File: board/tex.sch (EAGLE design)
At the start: 270 parts, among them K1 HLS8L-DC5V-S-C, K2 HLS8L-DC5V-S-C, K3 HLS8L-DC5V-S-C, K4 HLS8L-DC5V-S-C, Q41 FDD4141, U1 RELAY-S108T02PTH, U12 OPTO-LTV817, U13 OPTO-LTV817, U14 OPTO-LTV817, U15 OPTO-LTV817, U17 24LC32A, U18 IO-HC4051, U2 RELAY-S108T02PTH, U4 AZ23C5V1, Y1 32.768KHz

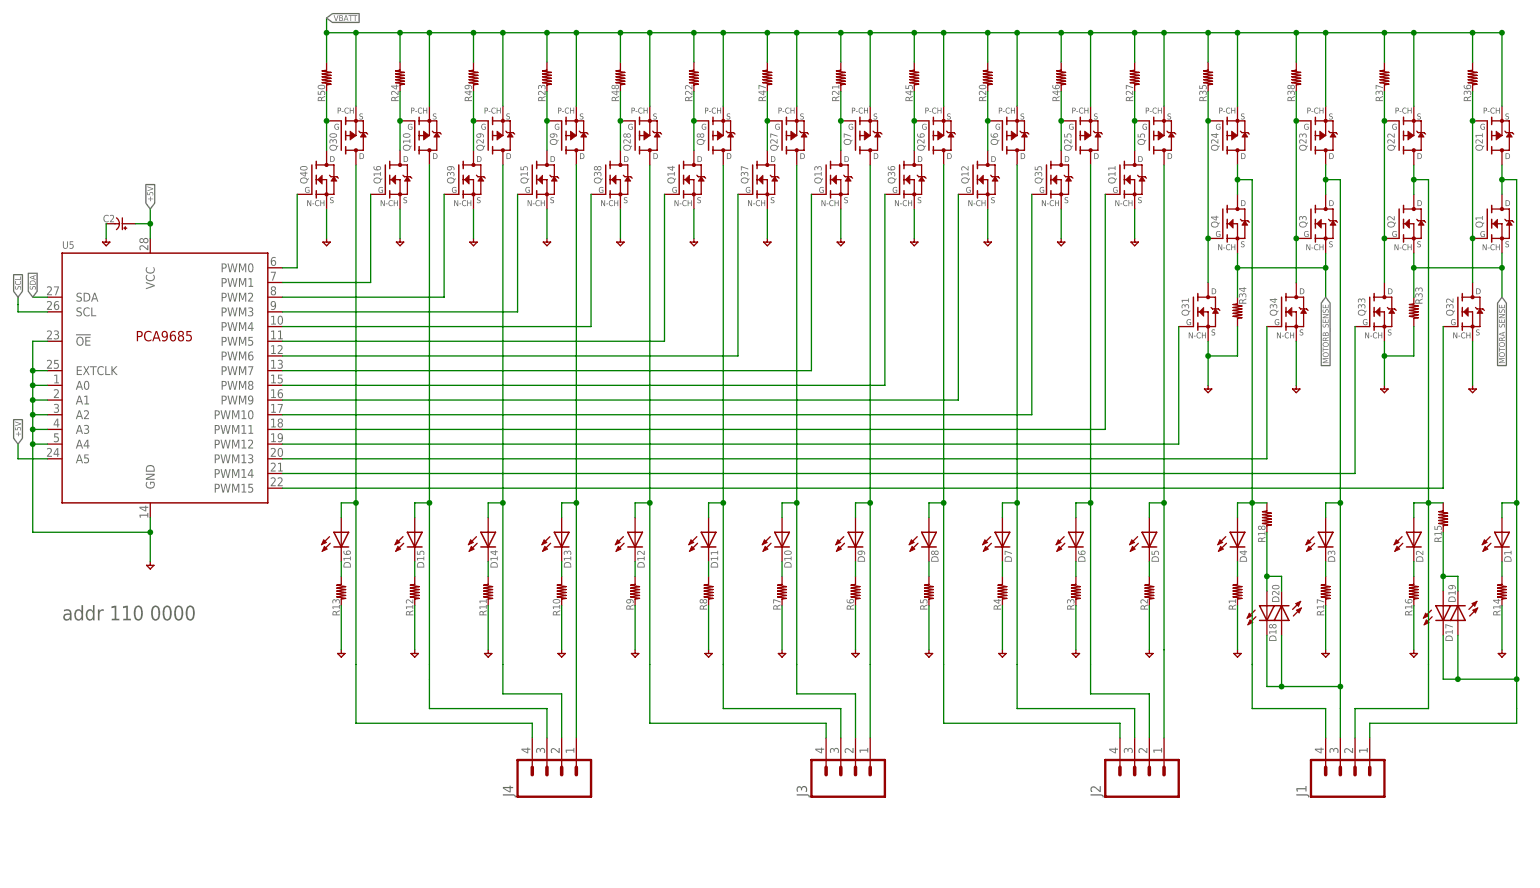
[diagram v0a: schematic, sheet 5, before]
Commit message: set R and C values
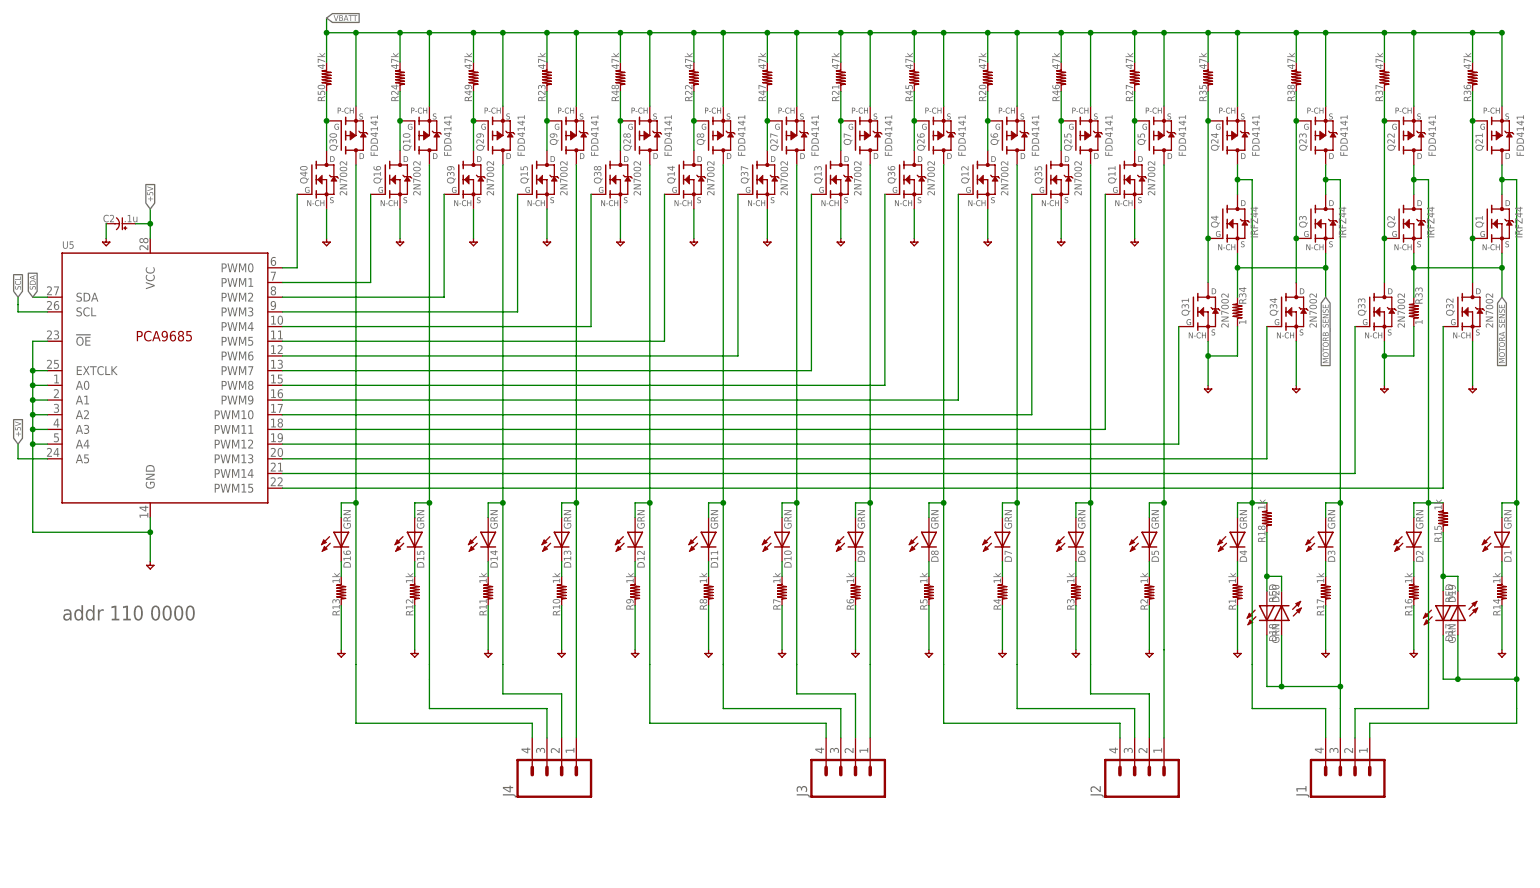
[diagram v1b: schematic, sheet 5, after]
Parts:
- C11, C15, C17, C18, C19, C2, C20, C21, C22, C23, C24, C25, C26, C27, C28, C29, C6, C7: value (none) -> .1u
- C13, C14: value .1u -> 10p
- D1, D10, D11, D12, D13, D14, D15, D16, D19, D2, D20, D25, D26, D27, D28, D29, D3, D30, D32, D4, D5, D6, D7, D8, D9: value (none) -> GRN
- D17, D18, D33: value (none) -> RED
- D21, D22, D23, D24, D35, D36: value (none) -> 1n4148
- D31: value (none) -> VZ=15.0
- D34: value (none) -> BLUE
- Q1, Q2, Q3, Q4: value (none) -> IRFZ44
- Q10, Q21, Q22, Q23, Q24, Q25, Q26, Q27, Q28, Q29, Q30, Q5, Q6, Q7, Q8, Q9: value (none) -> FDD4141
- Q11, Q12, Q13, Q14, Q15, Q16, Q17, Q18, Q19, Q20, Q31, Q32, Q33, Q34, Q35, Q36, Q37, Q38, Q39, Q40, Q42, Q43, Q44, Q45, Q46, Q47: value (none) -> 2N7002
- R1, R10, R11, R12, R13, R14, R15, R16, R17, R18, R2, R29, R3, R30, R31, R32, R4, R5, R58, R59, R6, R65, R66, R67, R68, R7, R8, R9: value (none) -> 1k
- R20, R21, R22, R23, R24, R27, R35, R36, R37, R38, R41, R42, R45, R46, R47, R48, R49, R50, R80, R81, R82, R83, R84, R85, R86, R88: value (none) -> 47k
- R25, R26, R60, R61, R62: value (none) -> 220
- R33, R34: value (none) -> 1
- R51: value (none) -> 10
- R64: value (none) -> 0
- R75: value (none) -> DNP
- R76, R87, R89, R90, R91, R92, R93, R94: value (none) -> 10k
- R78: value (none) -> 100

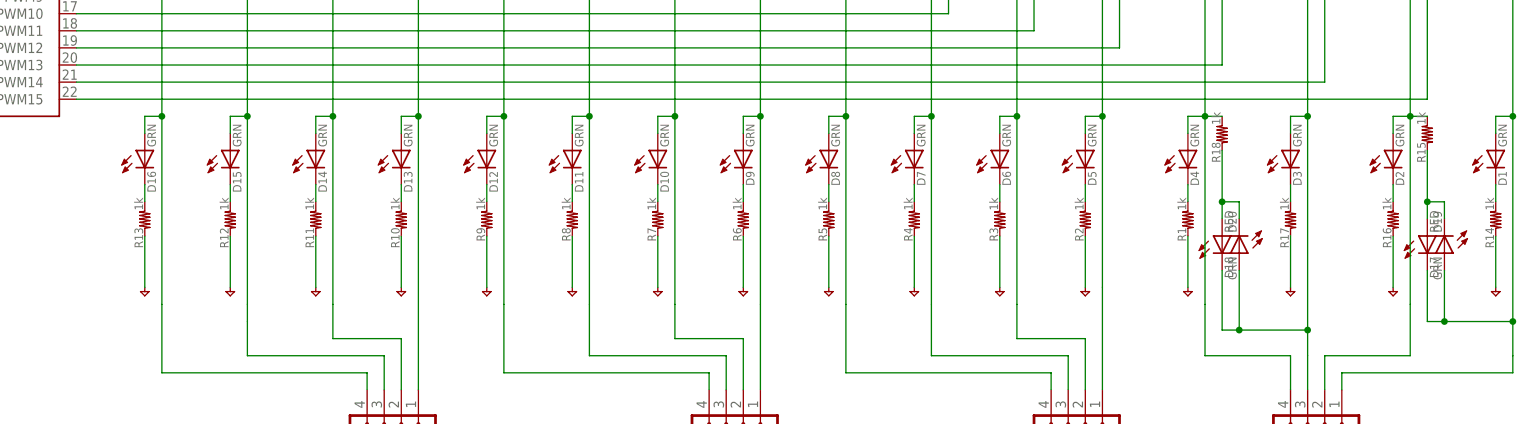
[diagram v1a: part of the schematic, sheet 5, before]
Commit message: changed connectors to match new lib naming
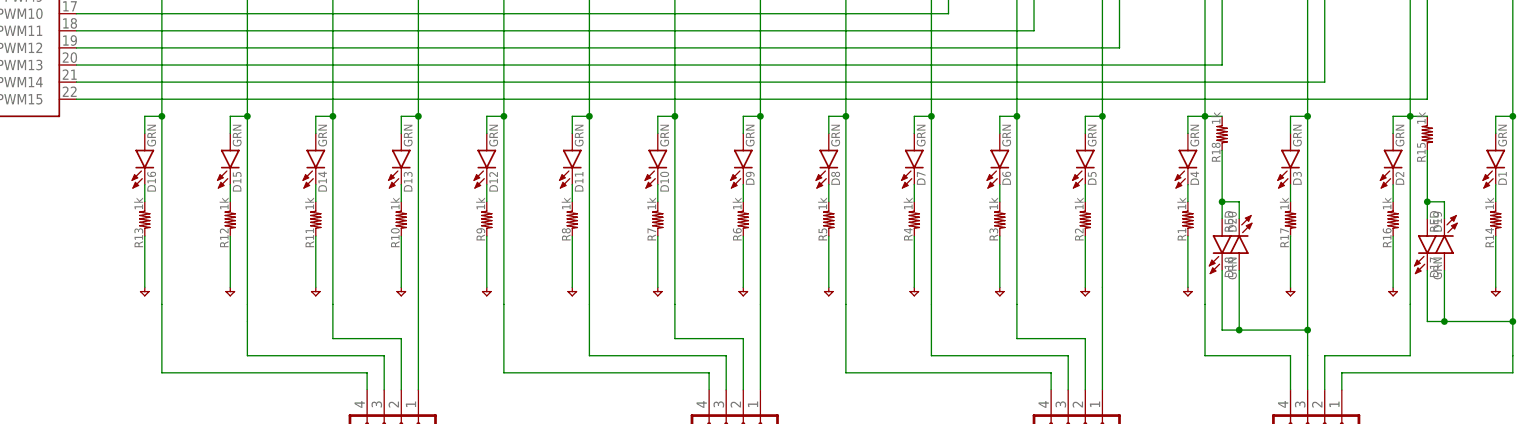
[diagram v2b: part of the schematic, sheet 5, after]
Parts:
- C1, C10, C11, C12, C15, C16, C17, C18, C19, C2, C20, C21, C22, C23, C24, C25, C26, C27, C28, C29, C3, C4, C5, C6, C7, C8, C9: device holla:C-USC0603 -> holla:C-0603
- C13, C14: value 10p -> 12p; device holla:C-USC0603 -> holla:C-0603
- J1, J14, J15, J2, J3, J4: device holla:M04-PLUGIN-SCREW -> holla:CONN-04-PLUGIN-SCREW
- J10, J27, J28, J7, J8, J9: device holla:M03-PLUGIN-SCREW -> holla:CONN-03-PLUGIN-SCREW
- J11: device holla:M04-0.1 -> holla:CONN-04-0.1
- J12: device holla:M02-0.1 -> holla:CONN-02-0.1
- J13, J17, J18: device holla:M05-PLUGIN-SCREW -> holla:CONN-05-PLUGIN-SCREW
- J16, J19, J29, J30: device holla:M06-PLUGIN-SCREW -> holla:CONN-06-PLUGIN-SCREW
- J20: device holla:M02-6.35MM -> holla:CONN-02-6.35MM
- J21, J22, J23, J24, J25, J26, J5, J6: device holla:M02-PLUGIN-SCREW -> holla:CONN-02-PLUGIN-SCREW
- R1, R10, R11, R12, R13, R14, R15, R16, R17, R18, R19, R2, R20, R21, R22, R23, R24, R25, R26, R27, R28, R29, R3, R30, R31, R32, R35, R36, R37, R38, R39, R4, R40, R41, R42, R43, R44, R45, R46, R47, R48, R49, R5, R50, R52, R53, R54, R55, R56, R57, R58, R59, R6, R60, R61, R62, R63, R64, R65, R66, R67, R68, R69, R7, R70, R71, R72, R73, R74, R75, R76, R77, R79, R8, R80, R81, R82, R83, R84, R85, R86, R87, R88, R89, R9, R90, R91, R92, R93, R94: device holla:R-US_R0603 -> holla:R-0603
- R33, R34, R51: device holla:R-US_R1210 -> holla:R-1210
- R78: value 100 -> 120; device holla:R-US_R0603 -> holla:R-0603
- renumbered B100 to B1

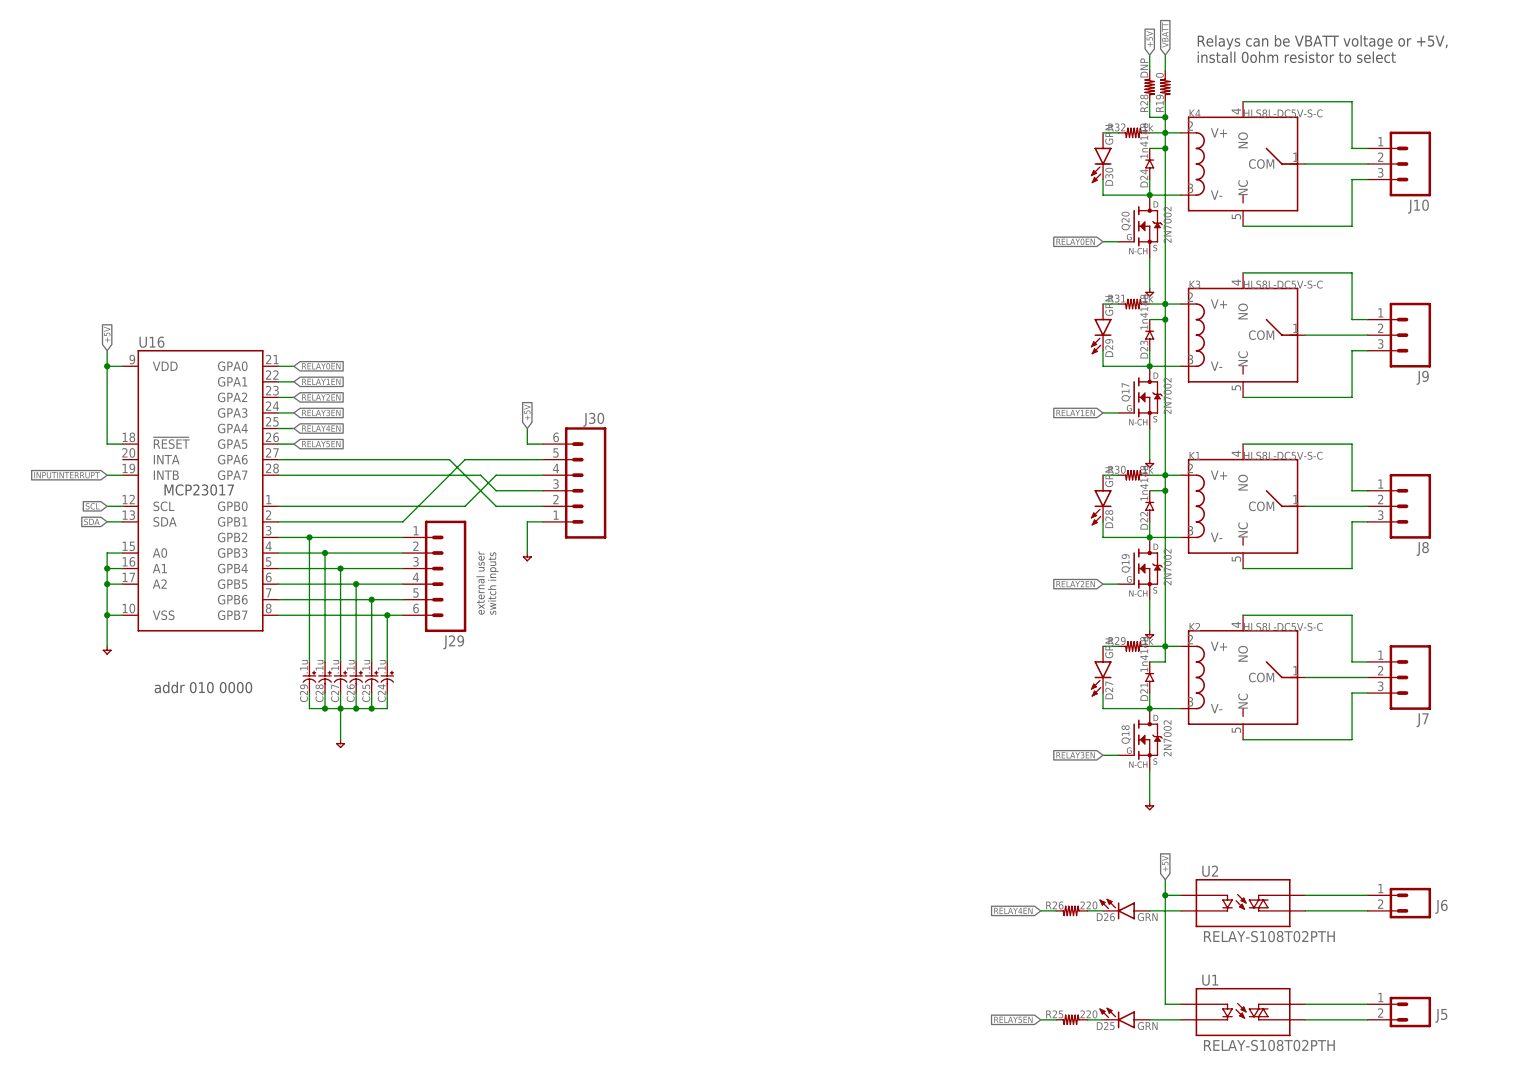
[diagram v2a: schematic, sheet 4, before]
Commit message: swapped relays for new part in holla lib
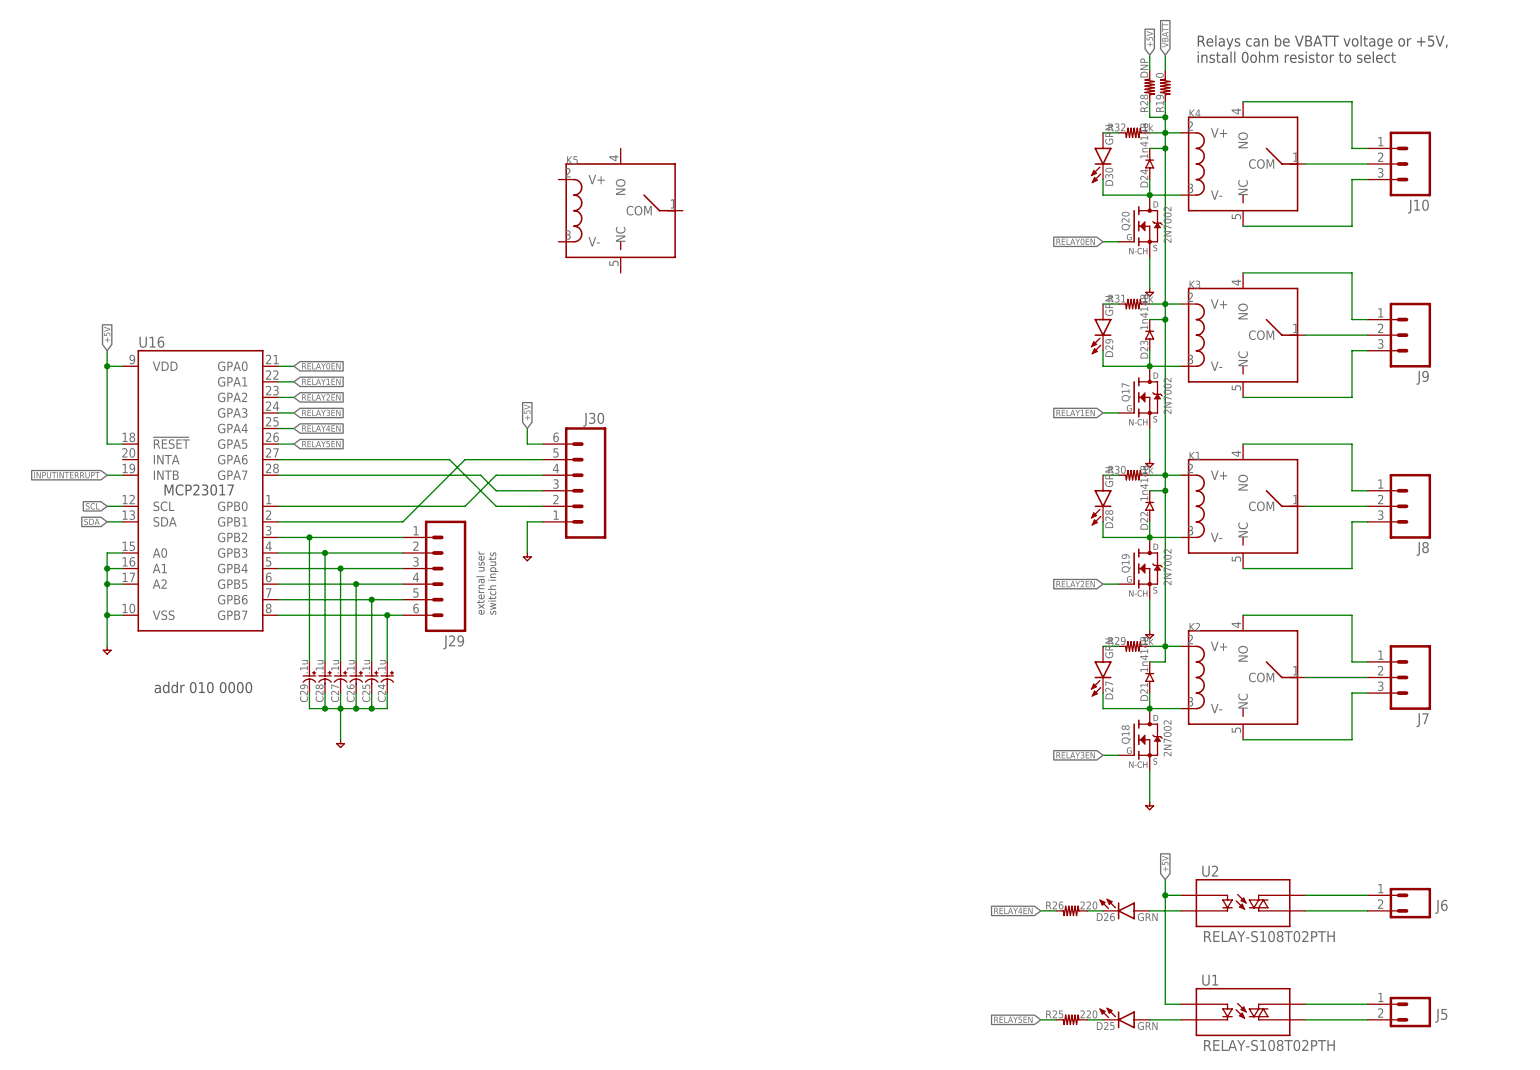
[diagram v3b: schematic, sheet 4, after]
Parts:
- added K5: (no value), holla:RELAY-SPST-19X15X15MM
- K1, K2, K3, K4: value HLS8L-DC5V-S-C -> (none); device holla:RELAY-HLS8L-DC5V-S-C(5P-19X15MM) -> holla:RELAY-SPST-19X15X15MM
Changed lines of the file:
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@@
 <part name="J14" library="holla" deviceset="CONN-04" device="-PLUGIN-SCREW"/>
 <part name="GND59" library="holla" deviceset="GND" device=""/>
-<part name="K4" library="holla" deviceset="RELAY-HLS8L-DC5V-S-C(5P-19X15MM)" device="" value="HLS8L-DC5V-S-C"/>
-<part name="K3" library="holla" deviceset="RELAY-HLS8L-DC5V-S-C(5P-19X15MM)" device="" value="HLS8L-DC5V-S-C"/>
-<part name="K1" library="holla" deviceset="RELAY-HLS8L-DC5V-S-C(5P-19X15MM)" device="" value="HLS8L-DC5V-S-C"/>
-<part name="K2" library="holla" deviceset="RELAY-HLS8L-DC5V-S-C(5P-19X15MM)" device="" value="HLS8L-DC5V-S-C"/>
+<part name="K1" library="holla" deviceset="RELAY-SPST" device="-19X15X15MM"/>
+<part name="K2" library="holla" deviceset="RELAY-SPST" device="-19X15X15MM"/>
+<part name="K3" library="holla" deviceset="RELAY-SPST" device="-19X15X15MM"/>
+<part name="K4" library="holla" deviceset="RELAY-SPST" device="-19X15X15MM"/>
+<part name="K5" library="holla" deviceset="RELAY-SPST" device="-19X15X15MM"/>
 <part name="J9" library="holla" deviceset="CONN-03" device="-PLUGIN-SCREW"/>
 <part name="J8" library="holla" deviceset="CONN-03" device="-PLUGIN-SCREW"/>
@@
 <wire x1="172.72" y1="141.605" x2="242.57" y2="141.605" width="0.1524" layer="94"/>
 <wire x1="242.57" y1="141.605" x2="242.57" y2="132.715" width="0.1524" layer="94"/>
-<text x="106.68" y="182.88" size="1.778" layer="94" align="top-left">ToDo List</text>
+<text x="58.42" y="195.58" size="1.778" layer="94" align="top-left">ToDo List</text>
 <text x="136.906" y="132.08" size="1.016" layer="94" rot="R180" align="center">ISENSE</text>
 <wire x1="140.97" y1="130.81" x2="135.89" y2="130.81" width="0.1524" layer="94"/>
@@
 <instance part="J30" gate="G$1" x="109.22" y="134.62" rot="MR0"/>
 <instance part="GND22" gate="1" x="101.6" y="119.38"/>
+<instance part="K5" gate="G$1" x="116.84" y="175.26"/>
 </instances>
 <busses>
